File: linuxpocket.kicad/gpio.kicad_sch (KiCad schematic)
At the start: 9 parts, among them J1 XDSM-1035-08-KT

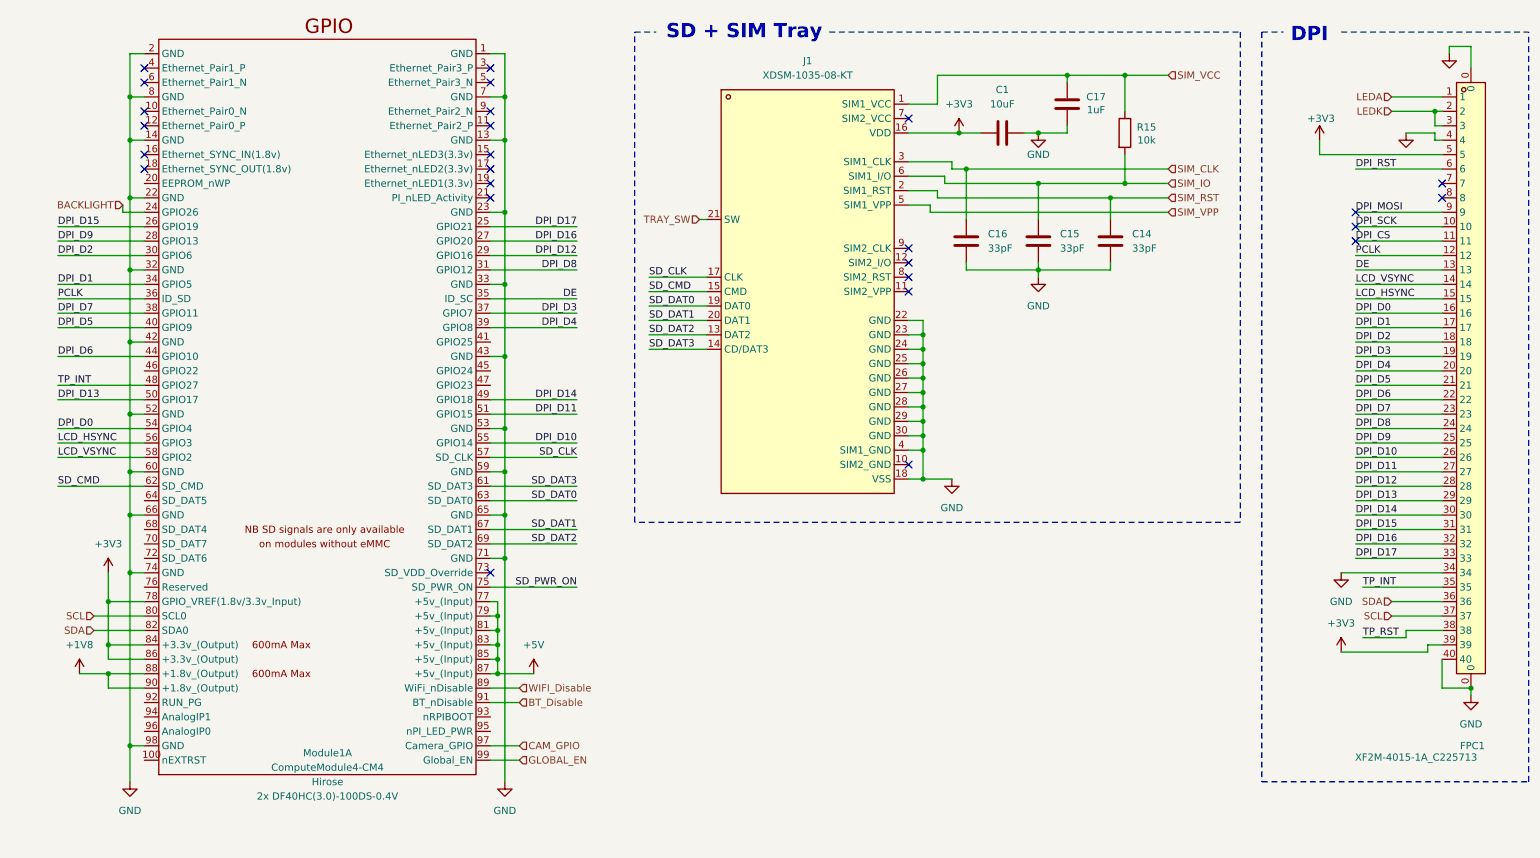
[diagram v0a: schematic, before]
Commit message: Add keyboard, improve many things etc.
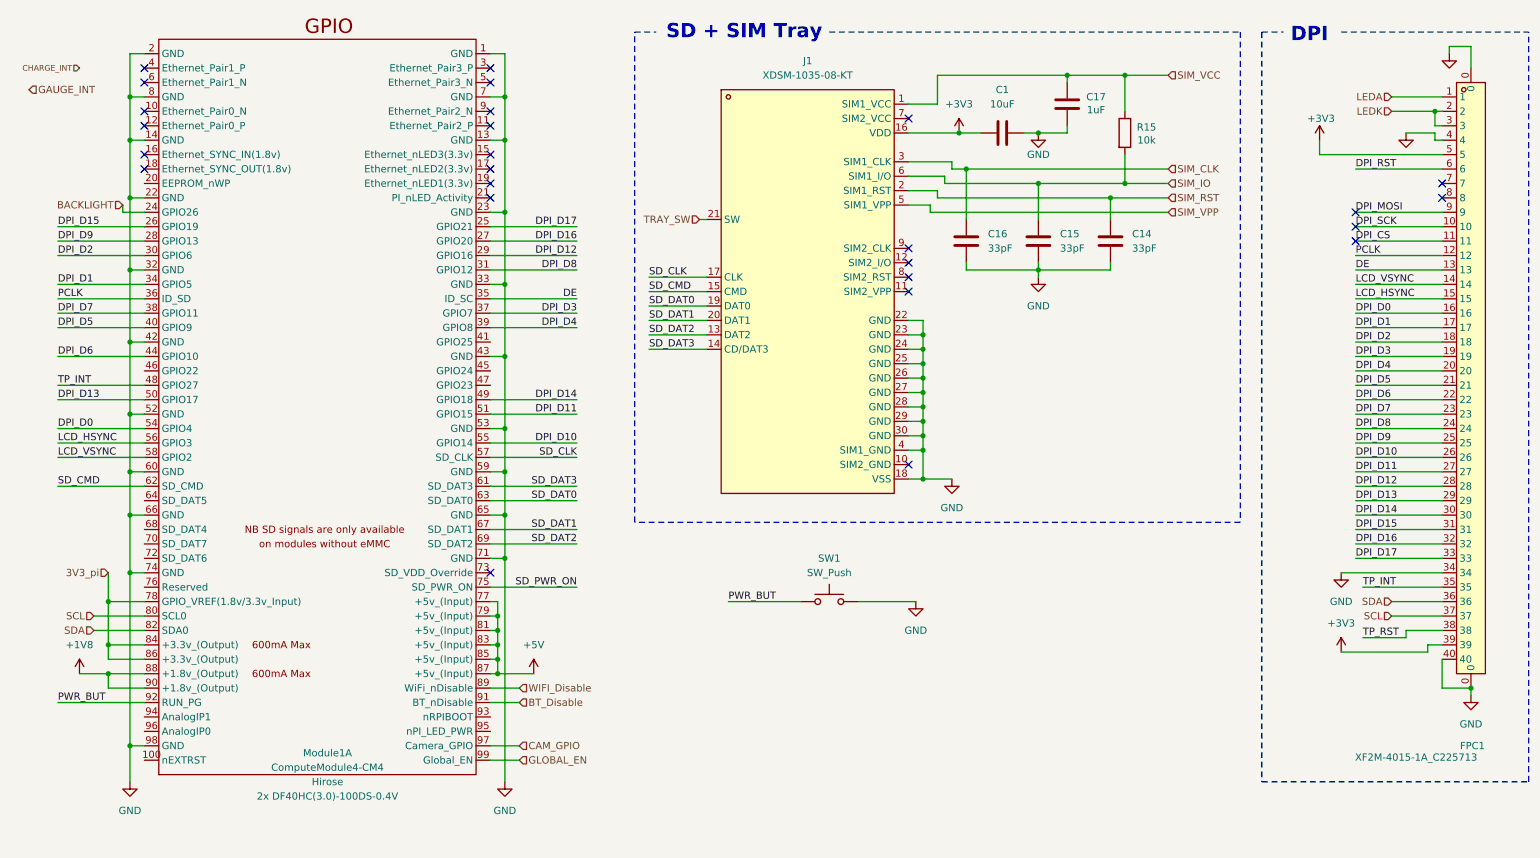
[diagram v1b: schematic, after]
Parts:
- added SW1: SW_Push, symbol Switch:SW_Push
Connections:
- net +3V3: no longer Module1.78 (GPIO_VREF(1.8v/3.3v_Input)), Module1.84 (+3.3v_(Output)), Module1.86 (+3.3v_(Output))
- net GND: now also SW1.2
- net PWR_BUT: now reaches Module1.92 (RUN_PG)
- net PWR_BUT: now also SW1.1
- new net 3V3_pi: Module1.78 (GPIO_VREF(1.8v/3.3v_Input)), Module1.84 (+3.3v_(Output)), Module1.86 (+3.3v_(Output))
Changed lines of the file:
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@@
 	(wire
 		(pts
+			(xy 139.7 118.11) (xy 152.4 118.11)
+		)
+		(stroke
+			(width 0)
+			(type default)
+		)
+	)
+	(wire
+		(pts
 			(xy 102.87 133.35) (xy 97.79 133.35)
 		)
@@
 	(wire
 		(pts
+			(xy 162.56 118.11) (xy 172.72 118.11)
+		)
+		(stroke
+			(width 0)
+			(type default)
+		)
+	)
+	(wire
+		(pts
 			(xy 125.73 68.58) (xy 135.89 68.58)
 		)
@@
 	(wire
 		(pts
+			(xy 21.59 135.89) (xy 36.83 135.89)
+		)
+		(stroke
+			(width 0)
+			(type default)
+		)
+	)
+	(wire
+		(pts
 			(xy 209.55 39.37) (xy 209.55 44.45)
 		)
@@
 		)
 	)
+	(label "PWR_BUT"
+		(at 139.7 118.11 0)
+		(fields_autoplaced yes)
+		(effects
+			(font
+				(size 1.27 1.27)
+			)
+			(justify left bottom)
+		)
+	)
 	(label "DPI_D6"
 		(at 250.19 82.55 0)
@@
 		)
 	)
+	(label "PWR_BUT"
+		(at 21.59 135.89 0)
+		(fields_autoplaced yes)
+		(effects
+			(font
+				(size 1.27 1.27)
+			)
+			(justify left bottom)
+		)
+	)
 	(label "DPI_D6"
 		(at 21.59 74.93 0)
@@
 		)
 	)
+	(hierarchical_label "CHARGE_INT"
+		(shape input)
+		(at 25.4 24.13 180)
+		(fields_autoplaced yes)
+		(effects
+			(font
+				(size 1 1)
+			)
+			(justify right)
+		)
+	)
 	(hierarchical_label "SIM_CLK"
 		(shape input)
@@
 		)
 	)
+	(hierarchical_label "3V3_pi"
+		(shape input)
+		(at 30.48 113.03 180)
+		(fields_autoplaced yes)
+		(effects
+			(font
+				(size 1.27 1.27)
+			)
+			(justify right)
+		)
+	)
 	(hierarchical_label "LEDA"
 		(shape input)
@@
 		)
 	)
+	(hierarchical_label "GAUGE_INT"
+		(shape input)
+		(at 16.51 27.94 0)
+		(fields_autoplaced yes)
+		(effects
+			(font
+				(size 1.27 1.27)
+			)
+			(justify left)
+		)
+	)
 	(hierarchical_label "BACKLIGHT"
 		(shape input)
@@
 	)
 	(symbol
+		(lib_id "Switch:SW_Push")
+		(at 157.48 118.11 0)
+		(unit 1)
+		(exclude_from_sim no)
+		(in_bom yes)
+		(on_board yes)
+		(dnp no)
+		(fields_autoplaced yes)
+		(property "Reference" "SW1"
+			(at 157.48 110.49 0)
+			(effects
+				(font
+					(size 1.27 1.27)
+				)
+			)
+		)
+		(property "Value" "SW_Push"
+			(at 157.48 113.03 0)
+			(effects
+				(font
+					(size 1.27 1.27)
+				)
+			)
+		)
+		(property "Footprint" ""
+			(at 157.48 113.03 0)
+			(effects
+				(font
+					(size 1.27 1.27)
+				)
+				(hide yes)
+			)
+		)
+		(property "Datasheet" "~"
+			(at 157.48 113.03 0)
+			(effects
+				(font
+					(size 1.27 1.27)
+				)
+				(hide yes)
+			)
+		)
+		(property "Description" "Push button switch, generic, two pins"
+			(at 157.48 118.11 0)
+			(effects
+				(font
+					(size 1.27 1.27)
+				)
+				(hide yes)
+			)
+		)
+		(pin "2"
+		)
+		(pin "1"
+		)
+		(instances
+			(project ""
+				(path "/de3771bf-b13a-459d-a957-6ff90f7da387/157d7587-4674-47d2-b2e3-79ed693e51a7"
+					(reference "SW1")
+					(unit 1)
+				)
+			)
+		)
+	)
+	(symbol
+		(lib_id "power:GND")
+		(at 172.72 118.11 0)
+		(unit 1)
+		(exclude_from_sim no)
+		(in_bom yes)
+		(on_board yes)
+		(dnp no)
+		(fields_autoplaced yes)
+		(property "Reference" "#PWR048"
+			(at 172.72 124.46 0)
+			(effects
+				(font
+					(size 1.27 1.27)
+				)
+				(hide yes)
+			)
+		)
+		(property "Value" "GND"
+			(at 172.72 123.19 0)
+			(effects
+				(font
+					(size 1.27 1.27)
+				)
+			)
+		)
+		(property "Footprint" ""
+			(at 172.72 118.11 0)
+			(effects
+				(font
+					(size 1.27 1.27)
+				)
+				(hide yes)
+			)
+		)
+		(property "Datasheet" ""
+			(at 172.72 118.11 0)
+			(effects
+				(font
+					(size 1.27 1.27)
+				)
+				(hide yes)
+			)
+		)
+		(property "Description" "Power symbol creates a global label with name \"GND\" , ground"
+			(at 172.72 118.11 0)
+			(effects
+				(font
+					(size 1.27 1.27)
+				)
+				(hide yes)
+			)
+		)
+		(pin "1"
+		)
+		(instances
+			(project ""
+				(path "/de3771bf-b13a-459d-a957-6ff90f7da387/157d7587-4674-47d2-b2e3-79ed693e51a7"
+					(reference "#PWR048")
+					(unit 1)
+				)
+			)
+		)
+	)
+	(symbol
 		(lib_id "power:+3V3")
 		(at 180.34 35.56 0)
@@
 					(unit 1)
 				)
-			)
-		)
-	)
-	(symbol
-		(lib_id "power:+3V3")
-		(at 30.48 113.03 0)
-		(unit 1)
-		(exclude_from_sim no)
-		(in_bom yes)
-		(on_board yes)
-		(dnp no)
-		(fields_autoplaced yes)
-		(property "Reference" "#PWR04"
-			(at 30.48 116.84 0)
-			(effects
-				(font
-					(size 1.27 1.27)
-				)
-				(hide yes)
-			)
-		)
-		(property "Value" "+3V3"
-			(at 30.48 107.95 0)
-			(effects
-				(font
-					(size 1.27 1.27)
-				)
-			)
-		)
-		(property "Footprint" ""
-			(at 30.48 113.03 0)
-			(effects
-				(font
-					(size 1.27 1.27)
-				)
-				(hide yes)
-			)
-		)
-		(property "Datasheet" ""
-			(at 30.48 113.03 0)
-			(effects
-				(font
-					(size 1.27 1.27)
-				)
-				(hide yes)
-			)
-		)
-		(property "Description" "Power symbol creates a global label with name \"+3V3\""
-			(at 30.48 113.03 0)
-			(effects
-				(font
-					(size 1.27 1.27)
-				)
-				(hide yes)
-			)
-		)
-		(pin "1"
-		)
-		(instances
-			(project "linuxpocket"
-				(path "/de3771bf-b13a-459d-a957-6ff90f7da387/157d7587-4674-47d2-b2e3-79ed693e51a7"
-					(reference "#PWR04")
-					(unit 1)
-				)

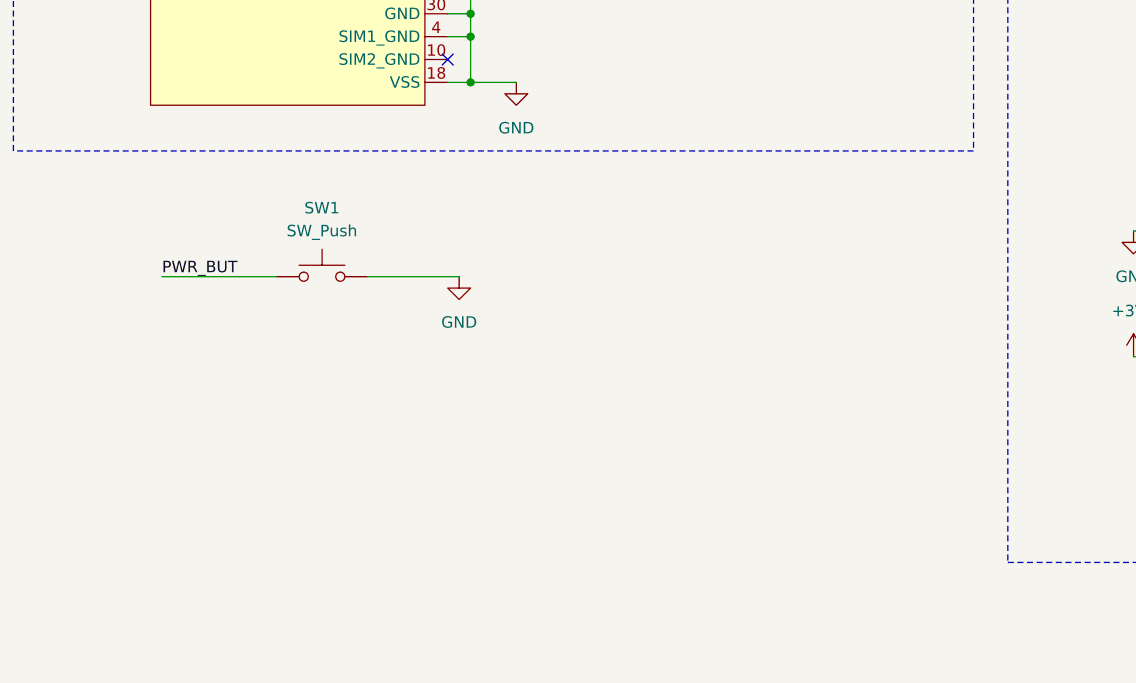
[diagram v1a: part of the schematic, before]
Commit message: Start with HDMI connector.
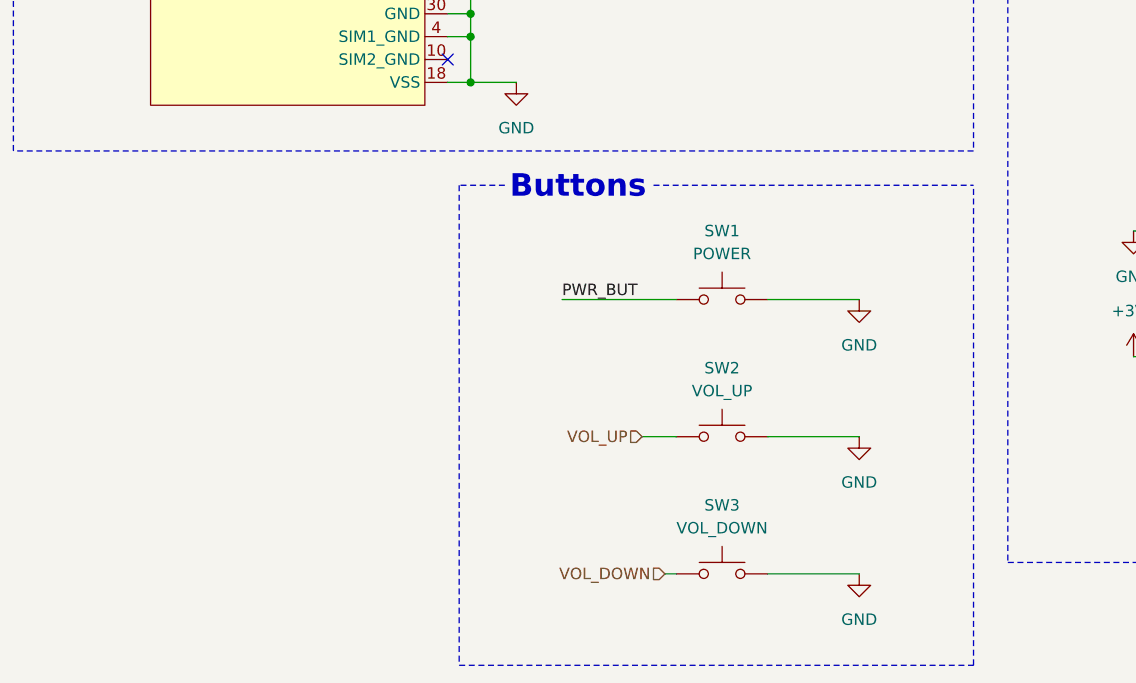
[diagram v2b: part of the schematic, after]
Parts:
- added SW2: VOL_UP, symbol Switch:SW_Push
- added SW3: VOL_DOWN, symbol Switch:SW_Push
- SW1: value SW_Push -> POWER
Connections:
- net GND: now also SW2.2, SW3.2
- new net VOL_DOWN: SW3.1
- new net VOL_UP: SW2.1
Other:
- note added: "Buttons"
- moved on the sheet: SW1

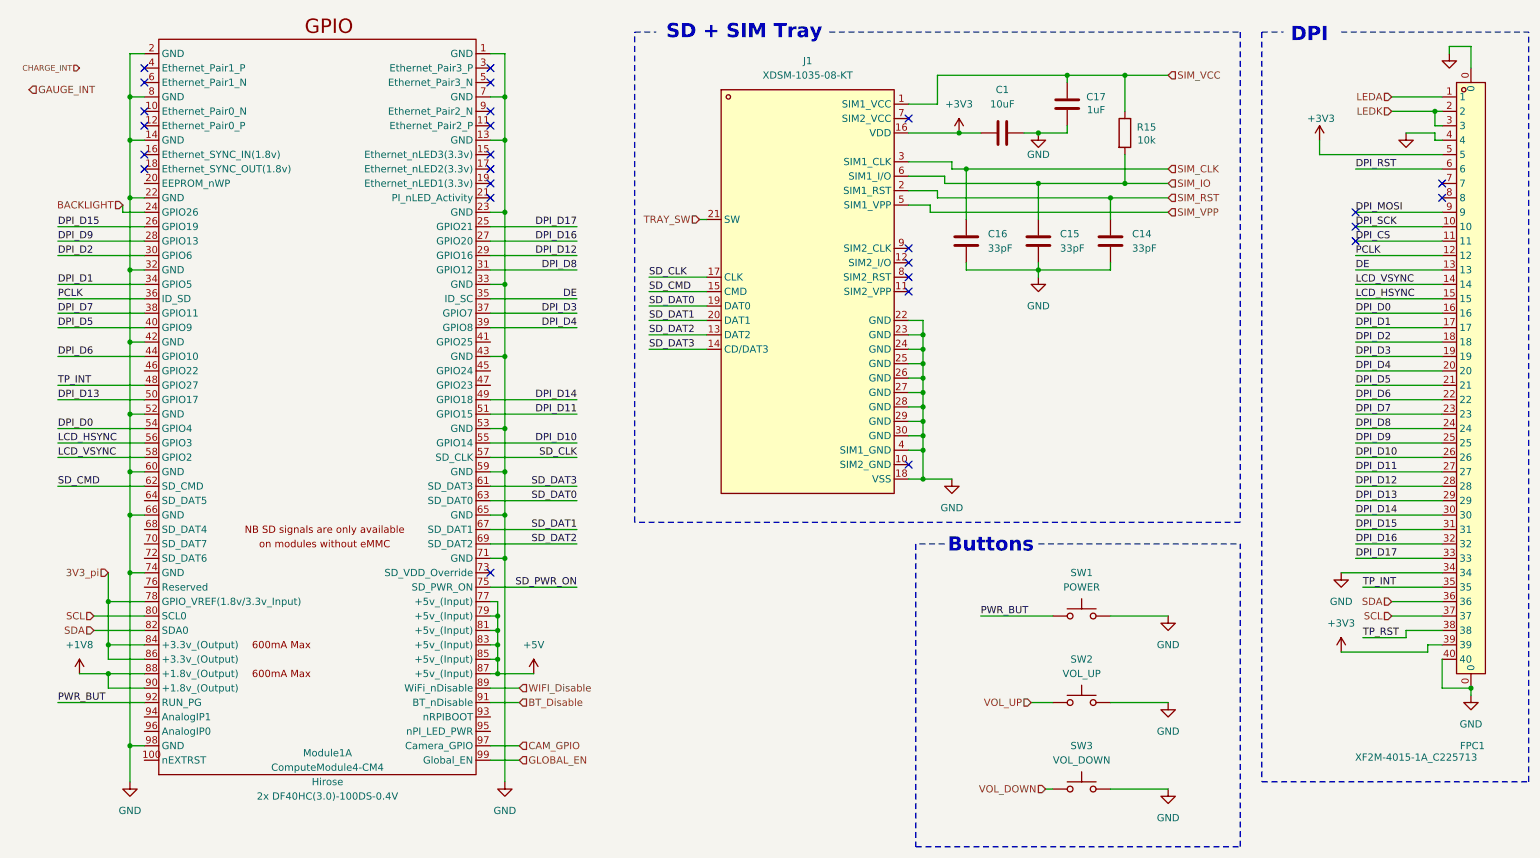
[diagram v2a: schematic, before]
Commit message: Add magnetometer #5. Add footprints to some symbols.
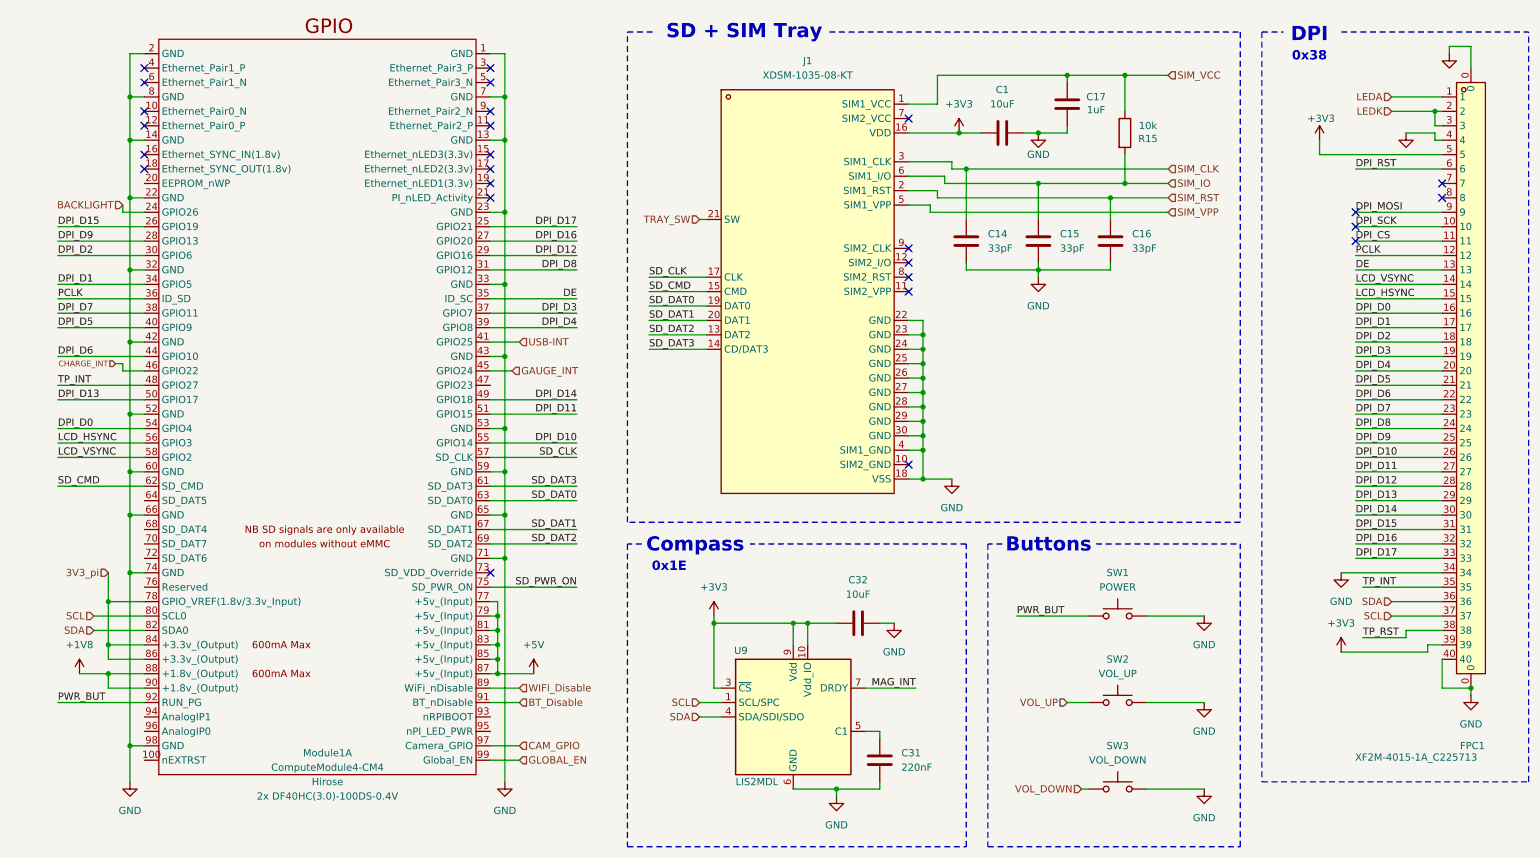
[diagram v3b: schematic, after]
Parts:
- added C31: 220nF, Capacitor_SMD:C_0402_1005Metric, symbol Device:C
- added C32: 10uF, Capacitor_SMD:C_0402_1005Metric, symbol Device:C
- added U9: LIS2MDL, Package_LGA:LGA-12_2x2mm_P0.5mm, symbol Sensor_Magnetic:LIS2MDL
- C14, C15, C16: footprint (none) -> Capacitor_SMD:C_0402_1005Metric; LCSC (none) -> C1562
- R15: footprint (none) -> Resistor_SMD:R_0402_1005Metric; LCSC (none) -> C25744
- SW1, SW2, SW3: footprint (none) -> linuxpocket:SW-SMD_GT-TC020B-H035-L05; LCSC (none) -> C17179534
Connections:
- net +3V3: now also C32.2, U9.10 (Vdd_IO), U9.3 (~{CS}), U9.9 (Vdd)
- net CHARGE_INT: now also Module1.46 (GPIO22)
- net GAUGE_INT: now also Module1.45 (GPIO24)
- net GND: now also C31.2, C32.1, U9.6 (GND), U9.8 (GND)
- net SCL: now also U9.1 (SCL/SPC)
- net SDA: now also U9.4 (SDA/SDI/SDO)
- net SIM_CLK: now also C14.1; no longer C16.1
- net SIM_RST: now also C16.1; no longer C14.1
- net USB-INT: now reaches Module1.41 (GPIO25)
- new net: C31.1, U9.5 (C1)
- new net MAG_INT: U9.7 (DRDY)
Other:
- note added: "0x1E"
- note added: "0x38"
- note added: "Compass"
- moved on the sheet: SW1
